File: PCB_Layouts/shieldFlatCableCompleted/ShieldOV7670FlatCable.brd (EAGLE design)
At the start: 70.8 x 57.9 mm, 14 parts, among them X1 332-20

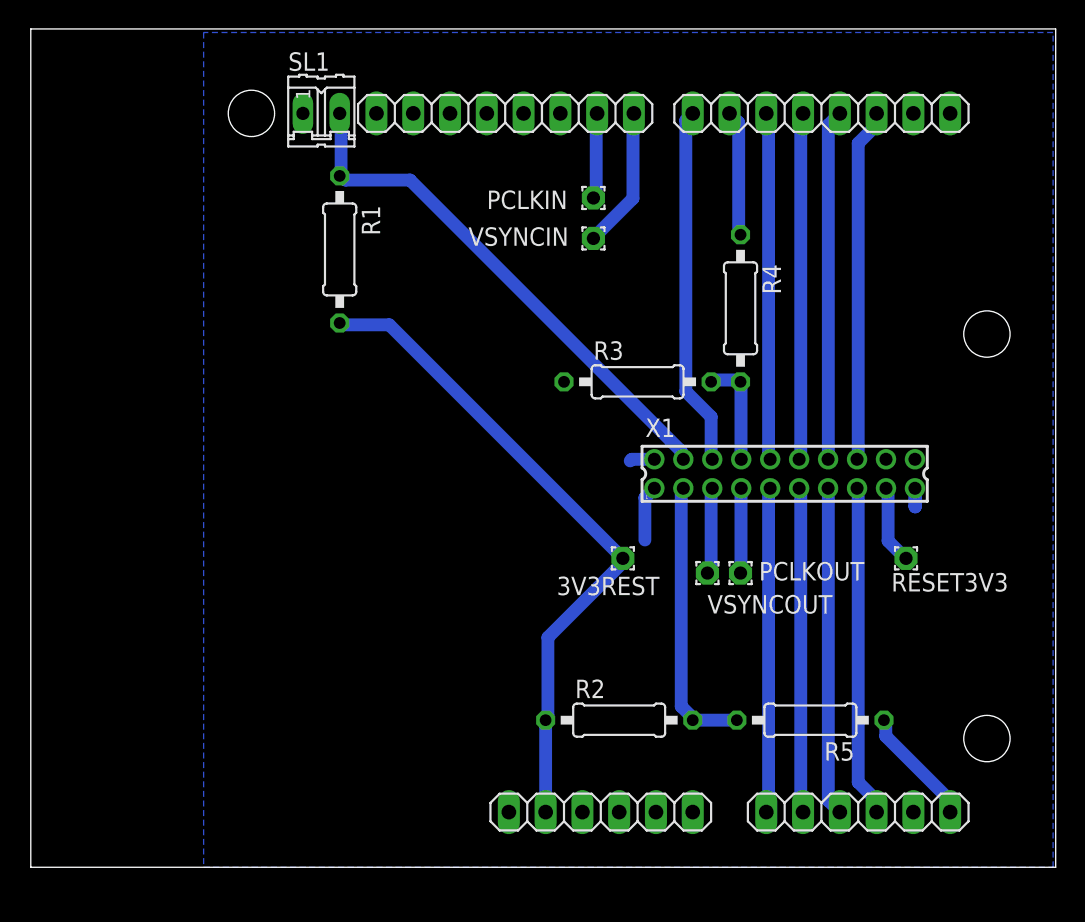
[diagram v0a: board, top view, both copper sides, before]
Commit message: Add layout folder w/ flatcable adapter shield for arduino uno
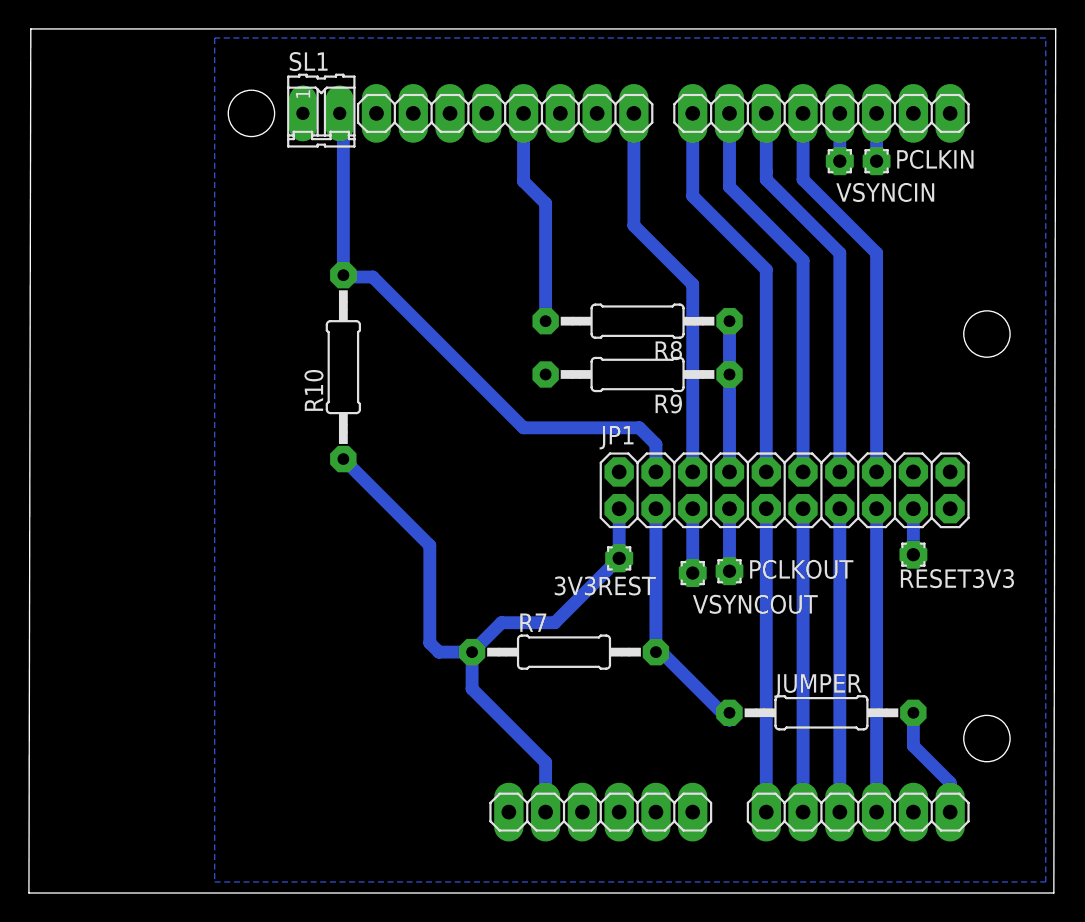
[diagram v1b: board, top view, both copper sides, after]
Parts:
- removed R1, R2, R3, R4, R5: (no value), rcl:0207/10
- removed X1: 332-20, con-garry:332-20
- added JP1: (no value), pinhead:2X10
- added JUMPER, R10, R7, R8, R9: (no value), rcl:0207/12
- moved PCLKIN 19.7 mm to (58.4, 47.5)
- moved VSYNCIN 17.8 mm to (55.9, 47.5)
- moved VSYNCOUT 1.02 mm to (45.7, 19.1)
- moved PCLKOUT 0.77 mm to (48.3, 19.2)
- moved RESET3V3 0.57 mm to (61.0, 20.3)
- moved 3V3REST 0.25 mm to (40.6, 20.1)
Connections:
- removed net N$9: IC1.19, R4.1
- new net N$7: IC1.24, R8.2
- net 3V3: now also JP1.1, R10.1, R7.1; no longer R1.2, R2.1, X1.1
- net D0: now also IC1.17, JP1.16; no longer IC1.15, X1.16
- net D1: now also JP1.15; no longer X1.15
- net D2: now also IC1.18, JP1.14; no longer IC1.16, X1.14
- net D3: now also JP1.13; no longer X1.13
- net D4: now also IC1.19, JP1.12; no longer IC1.17, X1.12
- net D5: now also JP1.11; no longer X1.11
- net D6: now also IC1.20, JP1.10; no longer IC1.18, X1.10
- net D7: now also JP1.9; no longer X1.9
- net GND: now also JP1.18, JP1.19, JP1.2, JP1.20, R9.2; no longer R3.1, X1.18, X1.19, X1.2, X1.20
- net HREF: now also IC1.21, JP1.6; no longer IC1.20, X1.6
- net N$1: now also IC1.15, PCLKIN.1; no longer IC1.21, VSYNCIN.1
- net N$2: now also IC1.16, VSYNCIN.1; no longer IC1.22, PCLKIN.1
- net N$3: now also JP1.5; no longer X1.5
- net N$4: now also JP1.7; no longer X1.7
- net N$5: now also JUMPER.2; no longer R5.1
- net N$6: now also JP1.17; no longer X1.17
- net SCL: now also JP1.3, JUMPER.1, R7.2; no longer R2.2, R5.2, X1.3
- net SDA: now also JP1.4, R10.2; no longer R1.1, X1.4
- net XCLK: now also JP1.8, R8.1, R9.1; no longer R3.2, R4.2, X1.8
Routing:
- net N$7: track 0.00 -> 15.0 mm
- net N$9: track 8.70 -> 0.00 mm
- net N$1: track 9.82 -> 3.30 mm
- net GND: track 4.30 -> 0.00 mm
- net XCLK: track 7.56 -> 10.8 mm
- net SDA: track 36.6 -> 39.8 mm
- net D4: track 24.0 -> 26.9 mm
- net D6: track 24.0 -> 26.9 mm
- net N$2: track 5.98 -> 3.30 mm
- net D2: track 24.2 -> 26.9 mm
- net D0: track 24.5 -> 26.9 mm
- net N$6: track 5.43 -> 3.18 mm
- net 3V3: track 49.8 -> 47.8 mm
- net D1: track 22.9 -> 21.0 mm
- net SCL: track 19.4 -> 17.6 mm
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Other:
- board size 70.8 x 57.9 mm -> 70.9 x 59.7 mm
